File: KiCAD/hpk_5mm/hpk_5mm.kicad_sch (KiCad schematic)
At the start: 4 parts, among them J1 Conn_01x03

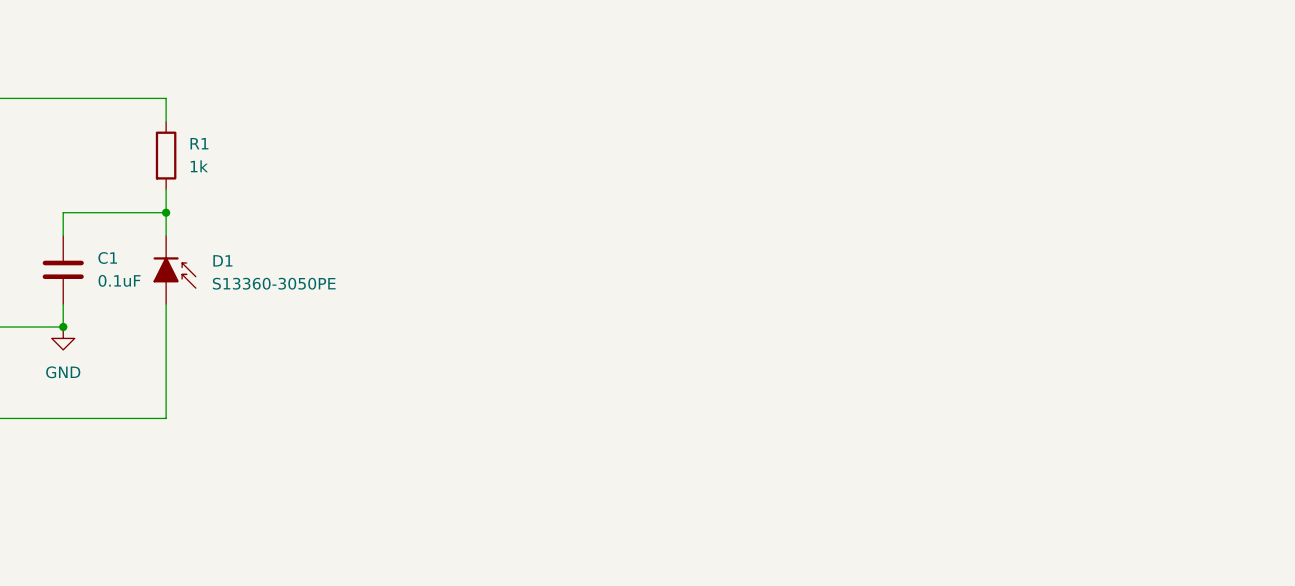
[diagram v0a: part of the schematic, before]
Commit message: adding TIA for test layout
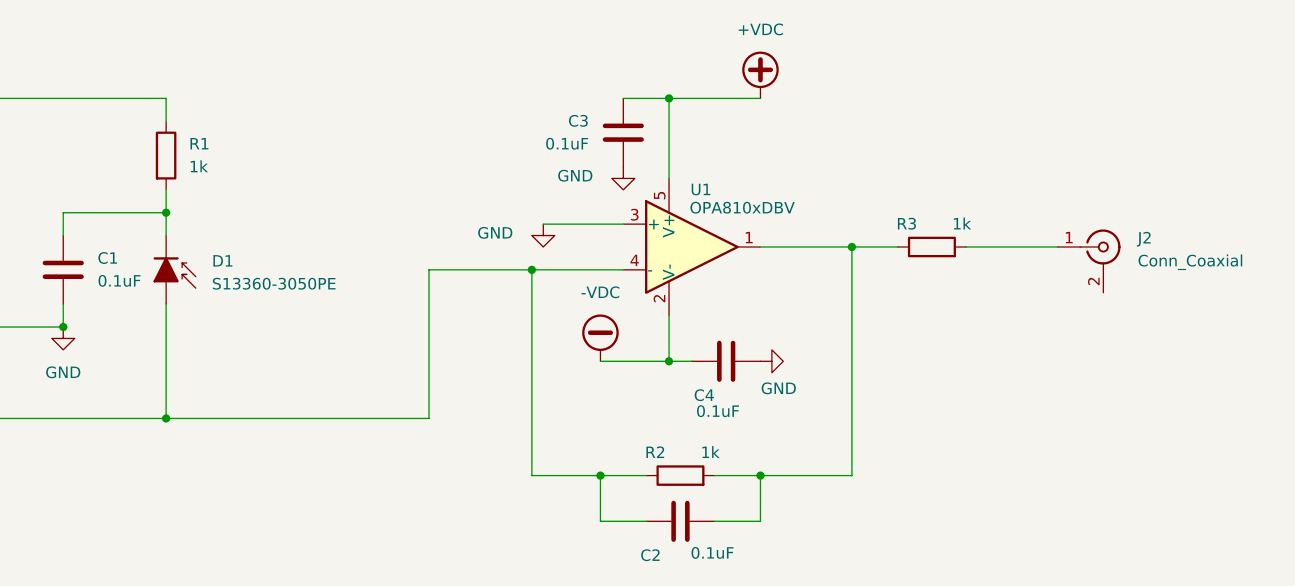
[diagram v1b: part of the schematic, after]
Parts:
- added C2, C3, C4: 0.1uF, Capacitor_SMD:C_0402_1005Metric, symbol Device:C
- added J2: Conn_Coaxial, symbol Connector:Conn_Coaxial
- added R2, R3: 1k, Resistor_SMD:R_0402_1005Metric, symbol Device:R
- added U1: OPA810xDBV, Package_TO_SOT_SMD:SOT-23-5, symbol Amplifier_Operational:OPA810xDBV
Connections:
- net GND: now also C3.2, C4.2, U1.3 (+)
- net at D1.2 (A), J1.3 (Pin_3): now also C2.1, R2.1, U1.4 (-)
- new net: C2.2, R2.2, R3.1, U1.1
- new net: J2.1 (In), R3.2
- new net +VDC: C3.1, U1.5 (V+)
- new net -VDC: C4.1, U1.2 (V-)

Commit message: trial 3-channel flexi
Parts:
- removed C1, C2, C3, C4: 0.1uF, Capacitor_SMD:C_0402_1005Metric, symbol Device:C
- removed D1: S13360-3050PE, my_sipm:s13360-3050pe, symbol Device:D_Photo_Filled
- removed J1: Conn_01x03, Connector_PinHeader_1.00mm:PinHeader_1x03_P1.00mm_Vertical, symbol Connector_Generic:Conn_01x03
- removed J2: Conn_Coaxial, symbol Connector:Conn_Coaxial
- removed R1, R2, R3: 1k, Resistor_SMD:R_0402_1005Metric, symbol Device:R
- removed U1: OPA810xDBV, Package_TO_SOT_SMD:SOT-23-5, symbol Amplifier_Operational:OPA810xDBV
- added J1: Conn_01x04, Connector_PinHeader_1.00mm:PinHeader_1x04_P1.00mm_Vertical, symbol Connector_Generic:Conn_01x04
- added J2: Conn_01x06, Connector_PinHeader_1.00mm:PinHeader_1x06_P1.00mm_Vertical, symbol Connector_Generic:Conn_01x06
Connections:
- net GND: now also J1.2 (Pin_2), J2.2 (Pin_2), J2.4 (Pin_4), J2.6 (Pin_6)
- new net sipm_tia1/V+: J1.1 (Pin_1)
- new net sipm_tia1/V-: J1.3 (Pin_3)
- new net sipm_tia1/VBIAS: J1.4 (Pin_4)
- new net sipm_tia1/VOUT: J2.1 (Pin_1)
- new net sipm_tia2/VOUT: J2.3 (Pin_3)
- new net sipm_tia3/VOUT: J2.5 (Pin_5)
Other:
- added sheet sipm_tia1 (sipm_tia.kicad_sch)
- added sheet sipm_tia2 (sipm_tia.kicad_sch)
- added sheet sipm_tia3 (sipm_tia.kicad_sch)

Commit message: flexi design
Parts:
- J1, J2: now not fitted
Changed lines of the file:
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@@
 		(exclude_from_sim no)
 		(in_bom yes)
-		(on_board yes)
-		(dnp no)
+		(on_board no)
+		(dnp yes)
 		(fields_autoplaced yes)
 		(property "Reference" "J1"
@@
 		(exclude_from_sim no)
 		(in_bom yes)
-		(on_board yes)
-		(dnp no)
+		(on_board no)
+		(dnp yes)
 		(fields_autoplaced yes)
 		(property "Reference" "J2"
